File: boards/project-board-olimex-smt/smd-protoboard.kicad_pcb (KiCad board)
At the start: 2 copper layers, 130 x 110 mm, 117 parts

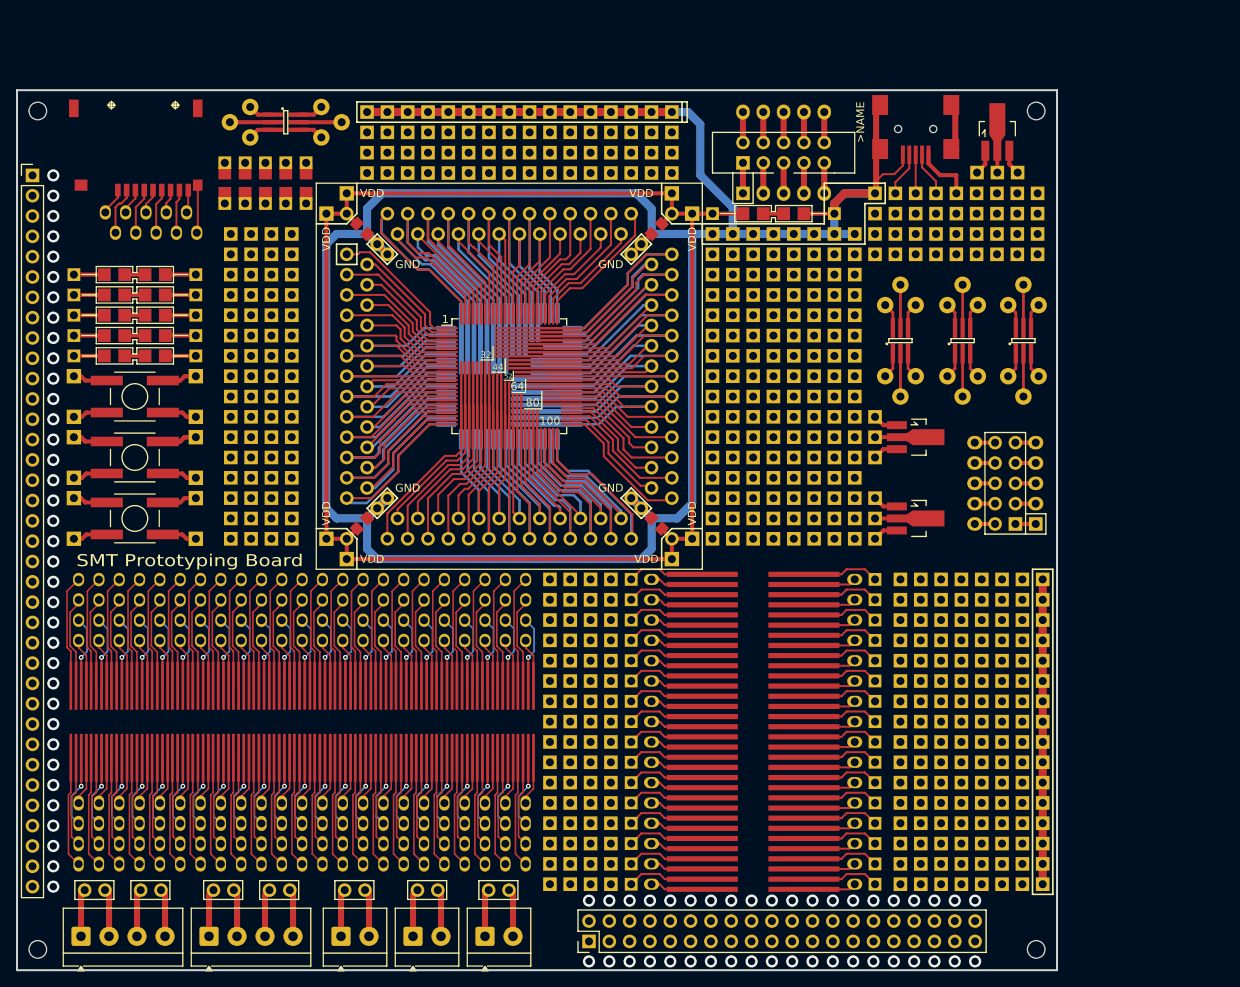
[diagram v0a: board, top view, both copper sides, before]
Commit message: rename to project boards and revise the olimex board a bit
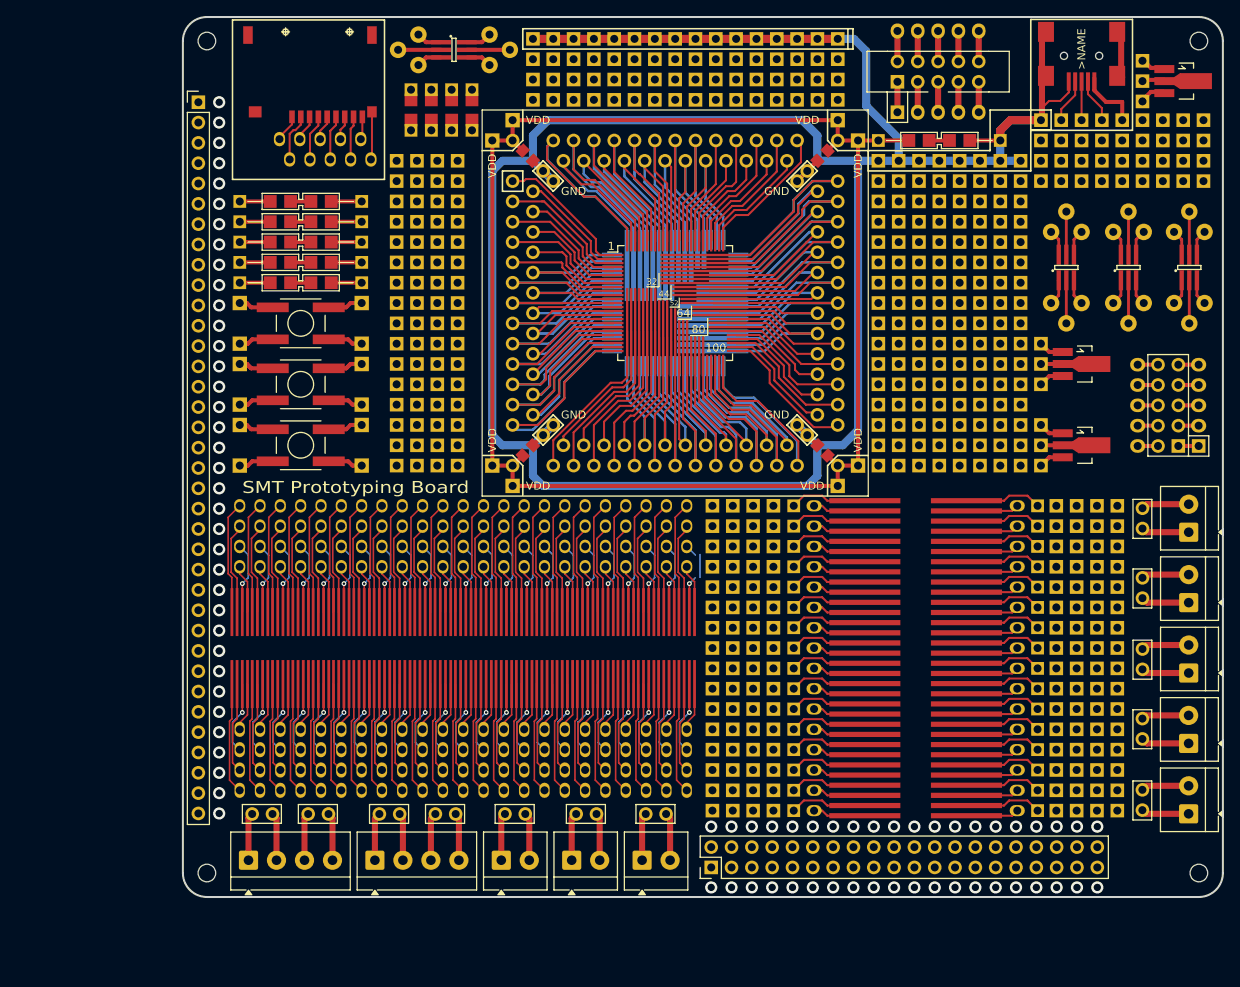
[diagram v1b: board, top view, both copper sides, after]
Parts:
- removed the ? at (105.3, 50.8)
- removed the ? at (200.0, 128.2)
- removed the ? at (200.0, 118.1)
- removed the ? at (200.0, 138.4)
- removed the ? at (200.0, 107.9)
- removed the REF** at (206.8, 41.7)
- removed the REF** at (82.0, 41.7)
- removed the REF** at (82.0, 146.5)
- removed the REF** at (206.8, 146.5)
- added REF**: TerminalBlock_4Ucon_1x02_P3.50mm_Horizontal, TerminalBlock_4Ucon:TerminalBlock_4Ucon_1x02_P3.50mm_Horizontal, F.Cu at (225.8, 112.0)
- added REF**: Proto_Pins_2_P2.54mm, Proto:Proto_Pins_2_P2.54mm, F.Cu at (220.0, 119.0)
- added REF**: MountingHole_2.2mm_M2, MountingHole:MountingHole_2.2mm_M2, F.Cu at (227.1, 33.0)
- added REF**: Proto_Pins_2_P2.54mm, Proto:Proto_Pins_2_P2.54mm, F.Cu at (220.1, 110.3)
- added REF**: MountingHole_2.2mm_M2, MountingHole:MountingHole_2.2mm_M2, F.Cu at (103.1, 137.0)
- added REF**: Proto_Pins_2_P2.54mm, Proto:Proto_Pins_2_P2.54mm, F.Cu at (220.0, 127.9)
- added REF**: TerminalBlock_4Ucon_1x02_P3.50mm_Horizontal, TerminalBlock_4Ucon:TerminalBlock_4Ucon_1x02_P3.50mm_Horizontal, F.Cu at (225.8, 120.8)
- added REF**: TerminalBlock_4Ucon_1x02_P3.50mm_Horizontal, TerminalBlock_4Ucon:TerminalBlock_4Ucon_1x02_P3.50mm_Horizontal, F.Cu at (225.8, 94.4)
- added REF**: Proto_Pins_2_P2.54mm, Proto:Proto_Pins_2_P2.54mm, F.Cu at (220.1, 92.7)
- added REF**: MountingHole_2.2mm_M2, MountingHole:MountingHole_2.2mm_M2, F.Cu at (227.1, 137.0)
- added REF**: MountingHole_2.2mm_M2, MountingHole:MountingHole_2.2mm_M2, F.Cu at (103.1, 33.0)
- added REF**: TerminalBlock_4Ucon_1x02_P3.50mm_Horizontal, TerminalBlock_4Ucon:TerminalBlock_4Ucon_1x02_P3.50mm_Horizontal, F.Cu at (225.8, 103.2)
- added REF**: Proto_Pins_2_P2.54mm, Proto:Proto_Pins_2_P2.54mm, F.Cu at (220.1, 101.4)
- added REF**: TerminalBlock_4Ucon_1x02_P3.50mm_Horizontal, TerminalBlock_4Ucon:TerminalBlock_4Ucon_1x02_P3.50mm_Horizontal, F.Cu at (225.8, 129.6)
- moved ? 24.1 mm to (225.1, 38.0), turned to -90 degrees
- moved ? 23.6 mm to (116.0, 35.1)
- moved REF** 23.0 mm to (117.0, 129.6)
- moved REF** 23.0 mm to (110.0, 129.6)
- moved REF** 23.0 mm to (108.3, 135.4)
- moved ? 22.9 mm to (134.0, 34.1)
- moved REF** 22.8 mm to (125.9, 129.6)
- moved REF** 22.8 mm to (132.9, 129.6)
- moved REF** 22.8 mm to (124.1, 135.4)
- moved >NAME 22.7 mm to (212.4, 34.0)
- moved ? 22.7 mm to (218.3, 61.3)
- moved ? 22.7 mm to (194.7, 45.4)
- moved ? 22.7 mm to (212.4, 83.5)
- moved ? 22.7 mm to (220.1, 50.5)
- moved ? 22.7 mm to (225.9, 61.3)
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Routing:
- net (no net): track 5835.7 -> 5857.4 mm
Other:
- outline, holes or cut-outs redrawn
